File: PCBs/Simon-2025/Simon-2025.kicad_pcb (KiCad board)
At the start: 2 copper layers, 65 x 65 mm, 21 parts, among them IC1 MSPM0G3507SDGS28R, J1 Conn_01x09, J2 Conn_01x05, SW1 SW_DPST, SW2 SW_DPST, SW3 SW_DPST, SW4 SW_DPST, SW6 SW_SPDT, U1 LIS2HH12

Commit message: Updated Simon PCB 2025
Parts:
- removed IC1: MSPM0G3507SDGS28R, ELEC327-Kicad:SOP50P490X110-28N
- added IC2: MSPM0G3507SPTR, ELEC327-Kicad:QFP50P900X900X160-48N, F.Cu at (82.5, 70.0)
- added REF**: RICE_OWL_LOGO, ELEC327-Kicad:RICE_OWL_LOGO, F.Cu at (66.5, 67.3)
- moved SW1 70.7 mm to (107.0, 93.0), turned to 0 degrees
- moved SW2 70.7 mm to (107.0, 42.0), turned to 180 degrees
- moved SW3 70.7 mm to (58.0, 42.0), turned to 180 degrees
- moved SW4 70.7 mm to (58.0, 93.0), turned to 0 degrees
- moved J1 59.4 mm to (54.4, 76.0), turned to 180 degrees
- moved BT1 50.2 mm to (76.0, 43.2), turned to -90 degrees
- moved BZ1 48.2 mm to (82.5, 90.8)
- moved J2 44.3 mm to (103.9, 61.7), turned to 0 degrees
- moved SW6 42.5 mm to (82.8, 46.2), turned to 0 degrees
- moved LED1 42.4 mm to (95.0, 80.0), turned to 0 degrees
- moved LED2 42.4 mm to (95.0, 55.0), turned to 180 degrees
- moved LED3 42.4 mm to (70.0, 55.0), turned to 180 degrees
- moved LED4 42.4 mm to (70.0, 80.0), turned to 0 degrees
- moved U1 17.5 mm to (91.2, 64.8), turned to 0 degrees
- moved C4 14.7 mm to (74.6, 72.8), turned to 180 degrees
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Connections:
- J1 pad 2: LED4_IO -> BUTTON4_IO
- J1 pad 3: LED3_IO -> BUTTON3_IO
- J1 pad 4: LED2_IO -> BUTTON2_IO
- J1 pad 5: LED1_IO -> BUTTON1_IO
- J1 pad 6: BUTTON4_IO -> LED4_IO
- J1 pad 7: BUTTON3_IO -> LED3_IO
- J1 pad 8: BUTTON2_IO -> LED2_IO
- J1 pad 9: BUTTON1_IO -> LED1_IO
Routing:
- net VDD: track 170.0 -> 127.0 mm, vias 10 -> 5
- net BUTTON4_IO: track 80.5 -> 51.9 mm, vias 1 -> 0
- net BUTTON2_IO: track 82.6 -> 107.3 mm
- net SWCLK: track 21.6 -> 34.5 mm
- net Net-(LED2-DOUT): track 32.0 -> 20.2 mm
- net SPI1_CS0: track 19.1 -> 7.76 mm
- net BUTTON1_IO: track 90.1 -> 101.4 mm
- net Net-(LED2-COUT): track 31.1 -> 20.2 mm
- net Net-(LED3-DOUT): track 36.2 -> 26.0 mm
- net Net-(LED3-COUT): track 40.0 -> 30.1 mm
- net SPI0_LED_PICO: track 19.6 -> 10.7 mm
- net SWDIO: track 20.0 -> 28.9 mm
- net ACC_INT: track 17.6 -> 9.67 mm, vias 2 -> 0
- net NRST: track 29.0 -> 35.3 mm, vias 2 -> 1
- net SPI0_LED_SCK: track 21.3 -> 16.0 mm
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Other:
- board text added: "GND VDD NRST SWDIO SWCLK"

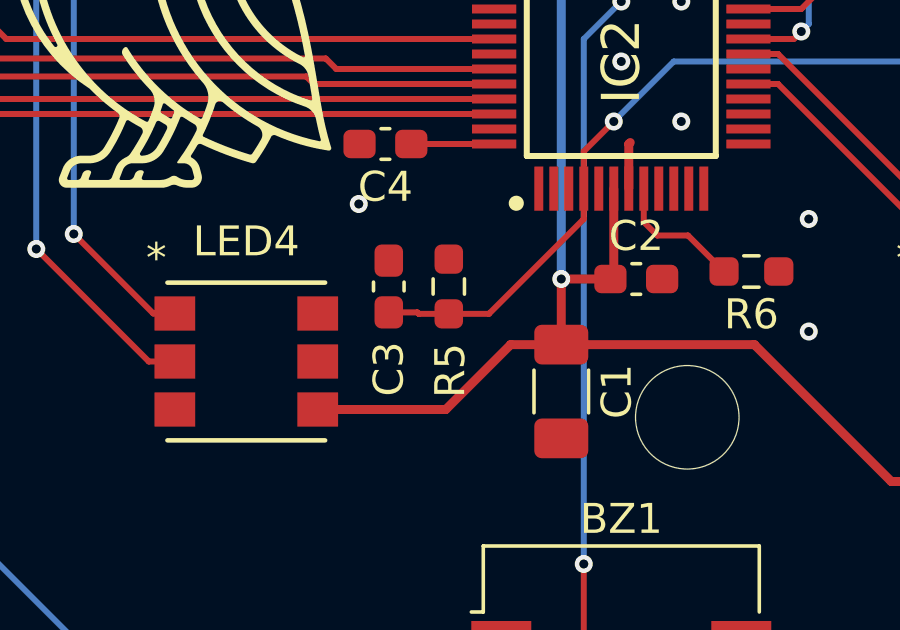
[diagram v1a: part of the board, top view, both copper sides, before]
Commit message: Fixed issue with NRST pullup resistor not being connected
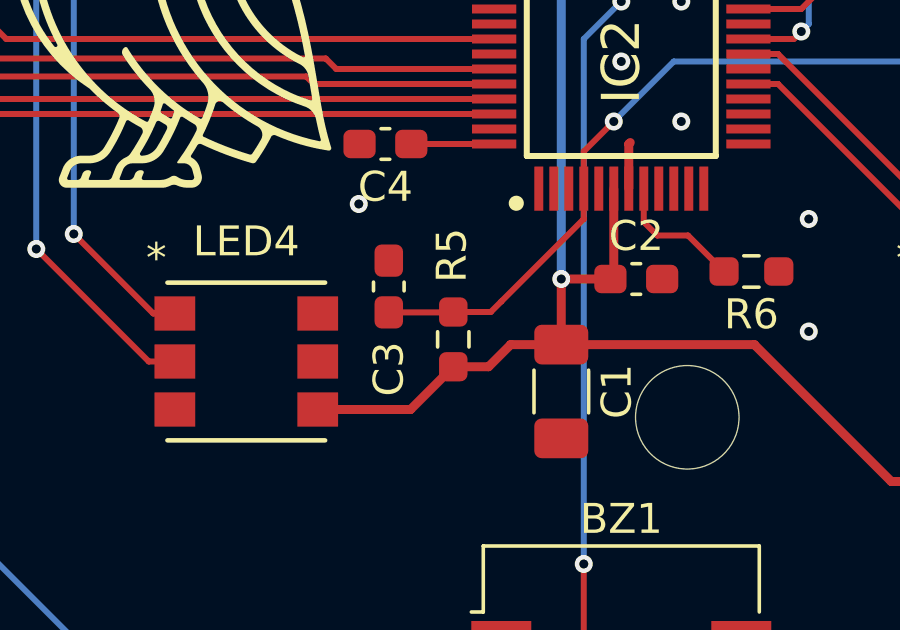
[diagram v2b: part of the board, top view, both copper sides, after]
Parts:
- moved R5 1.77 mm to (76.9, 79.3), turned to -90 degrees
